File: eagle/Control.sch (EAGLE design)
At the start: 9 parts, among them Q1 BD681

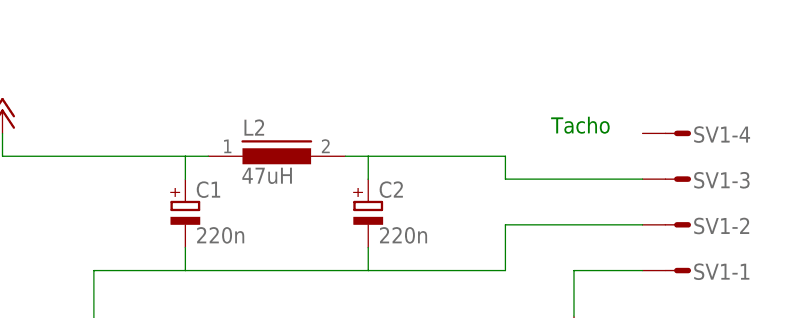
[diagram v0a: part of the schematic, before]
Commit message: some early state schematics and CAD files added
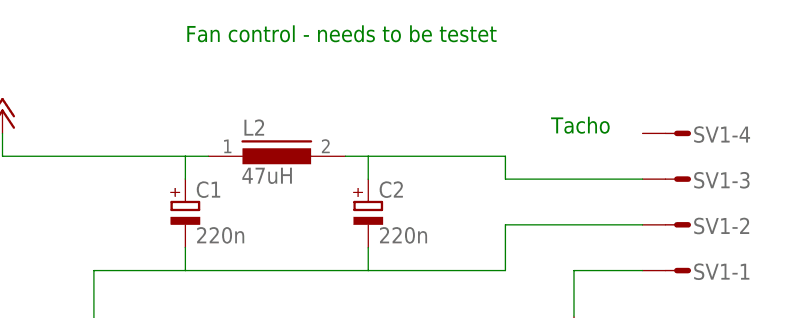
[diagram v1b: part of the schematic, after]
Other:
- note added: "Fan control - needs to be testet"
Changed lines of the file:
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@@
 <plain>
 <text x="66.04" y="109.22" size="1.778" layer="91">Tacho</text>
+<text x="25.4" y="119.38" size="1.778" layer="91">Fan control - needs to be testet</text>
 </plain>
 <instances>
